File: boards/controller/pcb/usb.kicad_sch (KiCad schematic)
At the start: 12 parts, among them J1 USB_C_Receptacle, U1 USBLC6-2SC6, U2 TCPP01-M12, U4 ISZ065N03L5SATMA1

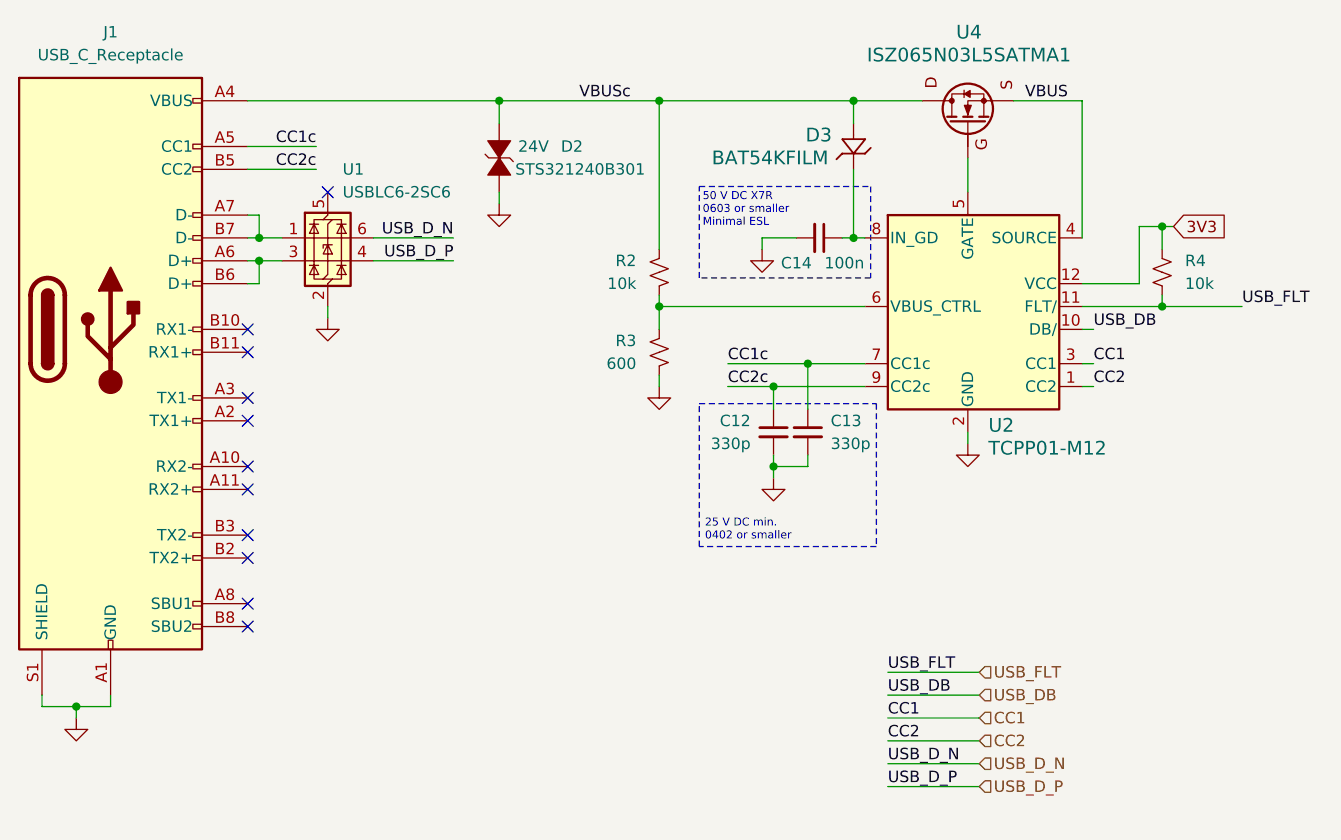
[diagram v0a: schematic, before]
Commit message: controller: Update PCB
Signed-off-by: Nicholas Loehrke <nicholasnloehrke@gmail.com>
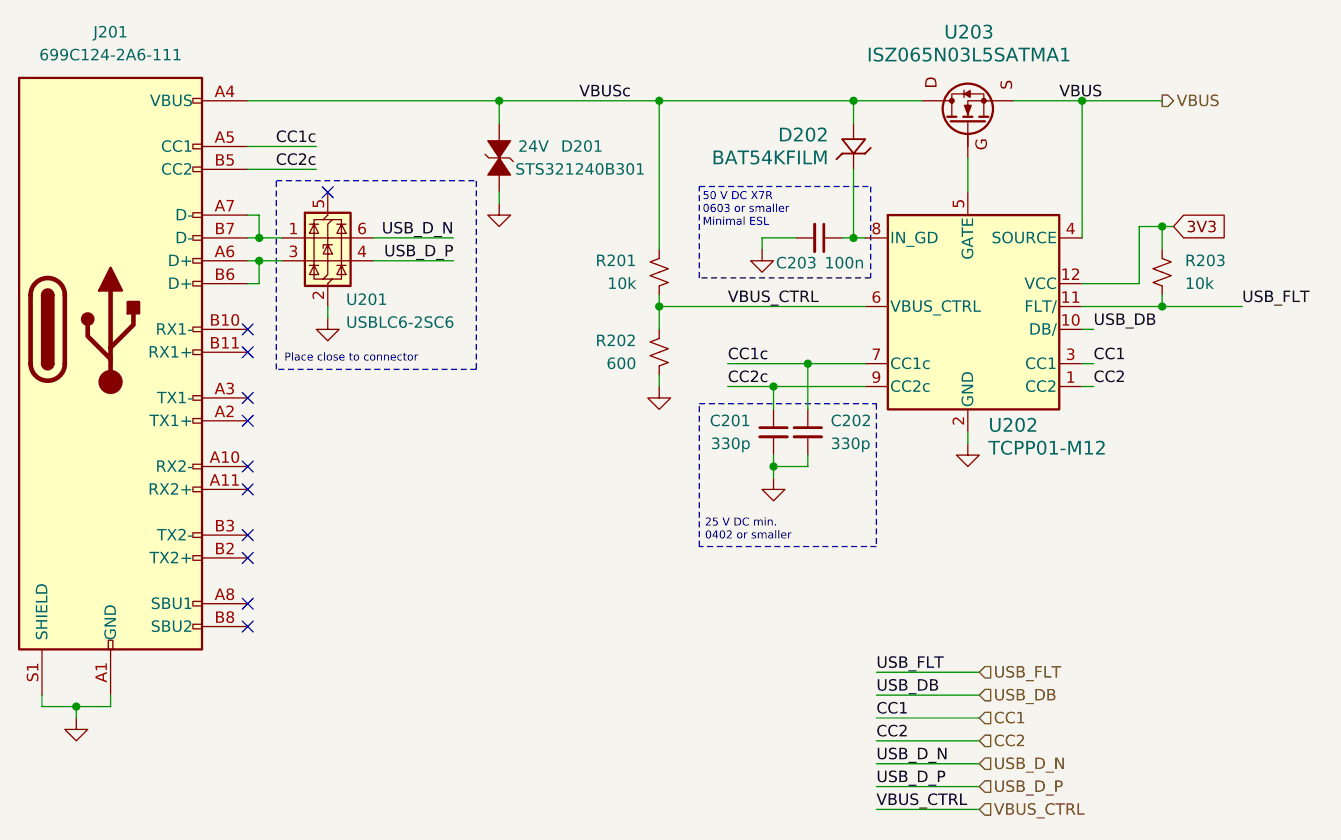
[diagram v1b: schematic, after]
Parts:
- J201: renamed from J1; value USB_C_Receptacle -> 699C124-2A6-111
- renumbered C12 to C201, C13 to C202, C14 to C203, D2 to D201, D3 to D202, R2 to R201, R3 to R202, R4 to R203, U1 to U201, U2 to U202, U4 to U203
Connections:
- net VBUS_CTRL: now reaches R201.2, R202.1, U202.6 (VBUS_CTRL)
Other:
- note added: "Place close to connector"
